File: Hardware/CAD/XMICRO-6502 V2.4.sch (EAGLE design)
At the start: 80 parts, among them Q1 2N4403, U1 74138, U10 7474, U11 74273, U12 74244, U13 74244, U14 74244, U15 74245, U16 74574, U17 7400, U18 7408, U19 7404, U2 74138, U20 W65C02S, U21 74244, U22 74138, U23 74148, U24 74244, U25 74244, U26 74273, U27 7432, U28 7432, U29 74257, U3 7400, U30 7474, U31 74LS14N, U4 7404, U5 74257, U6 74688, U7 74688, U8 74244, U9 7474, Y1 4MHz

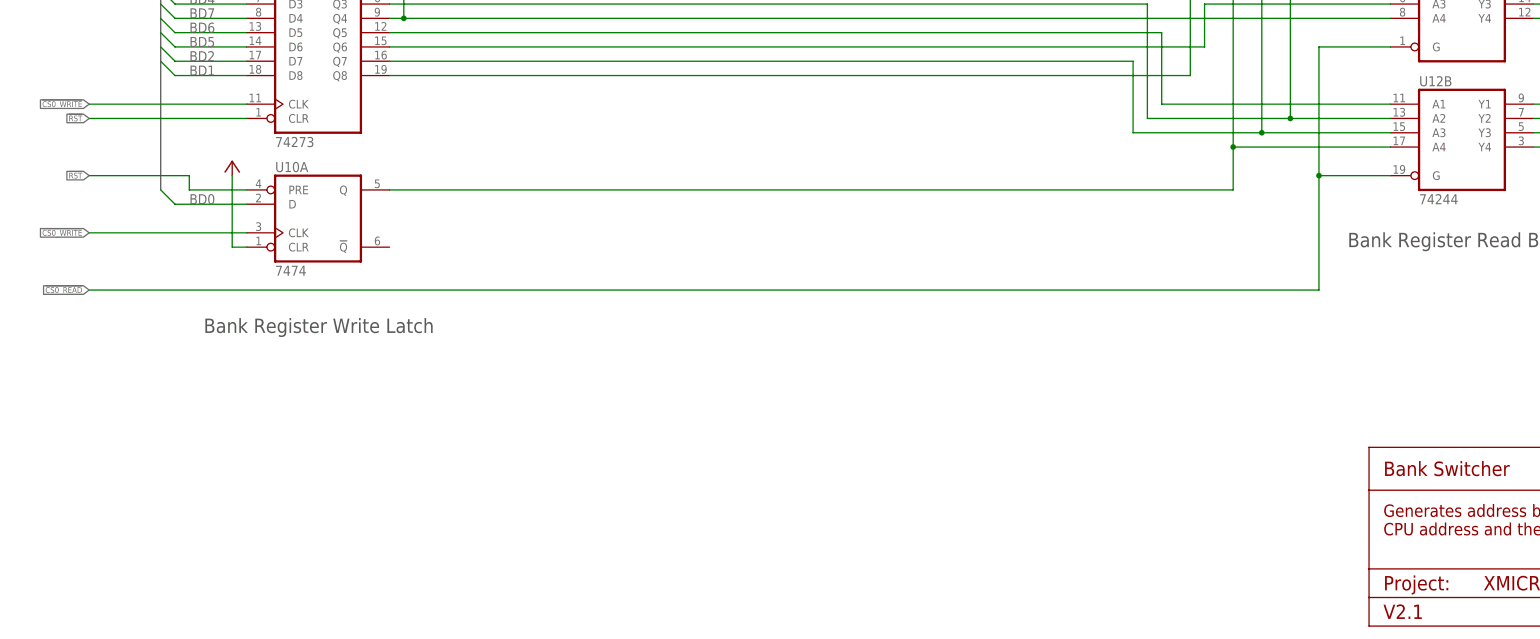
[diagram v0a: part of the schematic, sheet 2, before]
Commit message: Updated to V2.4 - made it necessary to manually clear DMA interrupts
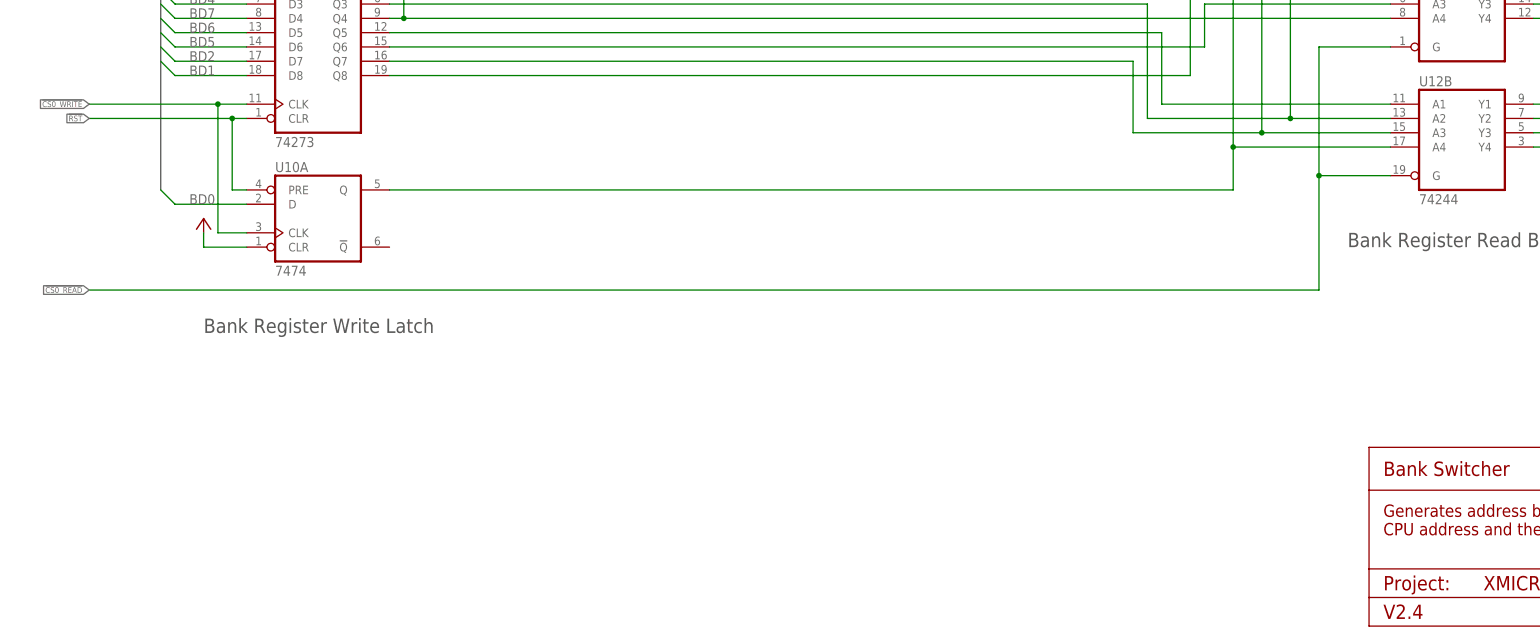
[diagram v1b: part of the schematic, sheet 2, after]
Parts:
- Y1: value 4MHz -> 12MHz
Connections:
- net !CS1_READ: now also U18B.I0
- net !IVP: no longer U18B.I0
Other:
- note added: "Interrupt is triggered upon !BUSACK!. Interrupt is cleared on reset or $X01 read (Interrupt Mask Register)"
- note added: "V2.4"
- note removed: "Interrupt is triggered upon !BUSACK!. Interrupt is cleared on reset or on the interrupt vector pull."
- note removed: "V2.1"
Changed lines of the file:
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@@
 <part name="GND12" library="supply1" deviceset="GND" device=""/>
 <part name="U17" library="74xx-us" deviceset="74*00" device="N" technology="LS" value="7400"/>
-<part name="Y1" library="Custom" deviceset="OSC-OE" device="" value="4MHz"/>
+<part name="Y1" library="Custom" deviceset="OSC-OE" device="" value="12MHz"/>
 <part name="P+1" library="supply1" deviceset="VCC" device=""/>
 <part name="GND14" library="supply1" deviceset="GND" device=""/>
@@
 <text x="306.07" y="10.16" size="2.54" layer="94" font="vector">Project:</text>
 <text x="306.07" y="30.48" size="2.54" layer="94" font="vector">CPU</text>
-<text x="306.07" y="5.08" size="2.54" layer="94" font="vector">V2.1</text>
+<text x="306.07" y="5.08" size="2.54" layer="94" font="vector">V2.4</text>
 <text x="379.73" y="10.16" size="2.54" layer="94" font="vector">Chris Weir</text>
 <text x="379.73" y="5.08" size="2.54" layer="94" font="vector">Sheet:</text>
@@
 <wire x1="402.59" y1="8.89" x2="377.19" y2="8.89" width="0" layer="94"/>
 <text x="306.07" y="10.16" size="2.54" layer="94" font="vector">Project:</text>
-<text x="306.07" y="5.08" size="2.54" layer="94" font="vector">V2.1</text>
+<text x="306.07" y="5.08" size="2.54" layer="94" font="vector">V2.4</text>
 <text x="379.73" y="10.16" size="2.54" layer="94" font="vector">Chris Weir</text>
 <text x="379.73" y="5.08" size="2.54" layer="94" font="vector">Sheet:</text>
@@
 <instance part="GND16" gate="1" x="236.22" y="167.64" smashed="yes"/>
 <instance part="U10" gate="A" x="116.84" y="76.2"/>
-<instance part="P+5" gate="VCC" x="101.6" y="86.36" smashed="yes"/>
+<instance part="P+5" gate="VCC" x="96.52" y="76.2" smashed="yes"/>
 <instance part="P+17" gate="VCC" x="101.6" y="124.46" smashed="yes"/>
 </instances>
@@
 <pinref part="U10" gate="A" pin="CLR"/>
 <pinref part="P+5" gate="VCC" pin="VCC"/>
-<wire x1="104.14" y1="71.12" x2="101.6" y2="71.12" width="0.1524" layer="91"/>
-<wire x1="101.6" y1="71.12" x2="101.6" y2="83.82" width="0.1524" layer="91"/>
+<wire x1="104.14" y1="71.12" x2="96.52" y2="71.12" width="0.1524" layer="91"/>
+<wire x1="96.52" y1="71.12" x2="96.52" y2="73.66" width="0.1524" layer="91"/>
 </segment>
 <segment>
@@
 <net name="!RST" class="0">
 <segment>
-<wire x1="104.14" y1="93.98" x2="76.2" y2="93.98" width="0.1524" layer="91"/>
+<wire x1="104.14" y1="93.98" x2="101.6" y2="93.98" width="0.1524" layer="91"/>
 <label x="76.2" y="93.98" size="1.016" layer="95" rot="R180" xref="yes"/>
 <pinref part="U11" gate="A" pin="CLR"/>
-<wire x1="104.14" y1="81.28" x2="93.98" y2="81.28" width="0.1524" layer="91"/>
-<wire x1="93.98" y1="81.28" x2="93.98" y2="83.82" width="0.1524" layer="91"/>
-<wire x1="93.98" y1="83.82" x2="76.2" y2="83.82" width="0.1524" layer="91"/>
-<label x="76.2" y="83.82" size="1.016" layer="95" rot="R180" xref="yes"/>
+<wire x1="101.6" y1="93.98" x2="76.2" y2="93.98" width="0.1524" layer="91"/>
+<wire x1="104.14" y1="81.28" x2="101.6" y2="81.28" width="0.1524" layer="91"/>
 <pinref part="U10" gate="A" pin="PRE"/>
+<wire x1="101.6" y1="81.28" x2="101.6" y2="93.98" width="0.1524" layer="91"/>
+<junction x="101.6" y="93.98"/>
 </segment>
 </net>
@@
 <segment>
 <pinref part="U11" gate="A" pin="CLK"/>
-<wire x1="76.2" y1="96.52" x2="104.14" y2="96.52" width="0.1524" layer="91"/>
+<wire x1="76.2" y1="96.52" x2="99.06" y2="96.52" width="0.1524" layer="91"/>
 <label x="76.2" y="96.52" size="1.016" layer="95" rot="R180" xref="yes"/>
-<wire x1="76.2" y1="73.66" x2="104.14" y2="73.66" width="0.1524" layer="91"/>
-<label x="76.2" y="73.66" size="1.016" layer="95" rot="R180" xref="yes"/>
+<wire x1="99.06" y1="96.52" x2="104.14" y2="96.52" width="0.1524" layer="91"/>
 <pinref part="U10" gate="A" pin="CLK"/>
+<wire x1="99.06" y1="73.66" x2="104.14" y2="73.66" width="0.1524" layer="91"/>
+<wire x1="99.06" y1="73.66" x2="99.06" y2="96.52" width="0.1524" layer="91"/>
+<junction x="99.06" y="96.52"/>
 </segment>
 </net>
@@
 <wire x1="402.59" y1="8.89" x2="377.19" y2="8.89" width="0" layer="94"/>
 <text x="306.07" y="10.16" size="2.54" layer="94" font="vector">Project:</text>
-<text x="306.07" y="5.08" size="2.54" layer="94" font="vector">V2.1</text>
+<text x="306.07" y="5.08" size="2.54" layer="94" font="vector">V2.4</text>
 <text x="379.73" y="10.16" size="2.54" layer="94" font="vector">Chris Weir</text>
 <text x="379.73" y="5.08" size="2.54" layer="94" font="vector">Sheet:</text>
@@
 <pinref part="U22" gate="A" pin="Y6"/>
 <wire x1="294.64" y1="104.14" x2="302.26" y2="104.14" width="0.1524" layer="91"/>
-<wire x1="302.26" y1="104.14" x2="312.42" y2="104.14" width="0.1524" layer="91"/>
-<junction x="302.26" y="104.14"/>
-<label x="320.04" y="104.14" size="1.016" layer="95" rot="R180" xref="yes"/>
 </segment>
 </net>
@@
 <description>DMA System</description>
 <plain>
-<text x="78.74" y="91.44" size="1.4224" layer="97" rot="MR180">Interrupt is triggered upon !BUSACK!.
-Interrupt is cleared on reset or on the interrupt vector pull.</text>
+<text x="76.2" y="93.98" size="1.4224" layer="97" rot="MR180">Interrupt is triggered upon !BUSACK!.
+Interrupt is cleared on reset or $X01 read (Interrupt Mask Register)</text>
 <frame x1="0" y1="0" x2="266.7" y2="203.2" columns="6" rows="5" layer="94"/>
 <text x="166.37" y="30.48" size="2.54" layer="94" font="vector">DMA System</text>
@@
 bus when safe, then acknowledges the request.
 An interrupt is triggered for each request.</text>
-<text x="78.74" y="96.52" size="2.54" layer="97" rot="MR180">DMA Interrupt</text>
+<text x="76.2" y="99.06" size="2.54" layer="97" rot="MR180">DMA Interrupt</text>
 <wire x1="163.83" y1="35.56" x2="262.89" y2="35.56" width="0" layer="94"/>
 <wire x1="262.89" y1="35.56" x2="262.89" y2="27.94" width="0" layer="94"/>
@@
 <wire x1="262.89" y1="8.89" x2="237.49" y2="8.89" width="0" layer="94"/>
 <text x="166.37" y="10.16" size="2.54" layer="94" font="vector">Project:</text>
-<text x="166.37" y="5.08" size="2.54" layer="94" font="vector">V2.1</text>
+<text x="166.37" y="5.08" size="2.54" layer="94" font="vector">V2.4</text>
 <text x="240.03" y="10.16" size="2.54" layer="94" font="vector">Chris Weir</text>
 <text x="240.03" y="5.08" size="2.54" layer="94" font="vector">Sheet:</text>
@@
 <text x="184.15" y="10.16" size="2.54" layer="94" font="vector">&gt;DRAWING_NAME</text>
 <text x="234.95" y="5.08" size="2.54" layer="94" font="vector" rot="MR0">&gt;LAST_DATE_TIME</text>
-<wire x1="76.2" y1="99.06" x2="76.2" y2="60.96" width="0.1524" layer="97" style="shortdash"/>
-<wire x1="76.2" y1="60.96" x2="187.96" y2="60.96" width="0.1524" layer="97" style="shortdash"/>
-<wire x1="187.96" y1="60.96" x2="187.96" y2="99.06" width="0.1524" layer="97" style="shortdash"/>
-<wire x1="187.96" y1="99.06" x2="76.2" y2="99.06" width="0.1524" layer="97" style="shortdash"/>
+<wire x1="73.66" y1="101.6" x2="73.66" y2="60.96" width="0.1524" layer="97" style="shortdash"/>
+<wire x1="73.66" y1="60.96" x2="187.96" y2="60.96" width="0.1524" layer="97" style="shortdash"/>
+<wire x1="187.96" y1="60.96" x2="187.96" y2="101.6" width="0.1524" layer="97" style="shortdash"/>
+<wire x1="187.96" y1="101.6" x2="73.66" y2="101.6" width="0.1524" layer="97" style="shortdash"/>
 </plain>
 <instances>
 <instance part="U10" gate="B" x="147.32" y="76.2"/>
 <instance part="U18" gate="B" x="109.22" y="71.12"/>
-<instance part="P+11" gate="VCC" x="132.08" y="86.36" smashed="yes" rot="MR0">
-<attribute name="VALUE" x="129.54" y="87.63" size="1.778" layer="96"/>
-</instance>
+<instance part="P+11" gate="VCC" x="132.08" y="86.36" smashed="yes" rot="MR0"/>
 <instance part="U9" gate="A" x="134.62" y="142.24"/>
-<instance part="P+16" gate="VCC" x="119.38" y="152.4" smashed="yes" rot="MR0">
-<attribute name="VALUE" x="116.84" y="153.67" size="1.778" layer="96"/>
-</instance>
+<instance part="P+16" gate="VCC" x="119.38" y="152.4" smashed="yes" rot="MR0"/>
 <instance part="U4" gate="E" x="66.04" y="149.86"/>
 <instance part="U18" gate="A" x="93.98" y="144.78"/>
 <instance part="U9" gate="B" x="193.04" y="142.24"/>
-<instance part="GND7" gate="1" x="177.8" y="132.08" rot="MR0"/>
+<instance part="GND7" gate="1" x="177.8" y="132.08" smashed="yes" rot="MR0"/>
 <instance part="U4" gate="F" x="66.04" y="129.54"/>
 <instance part="U4" gate="B" x="88.9" y="129.54"/>
@@
 </segment>
 </net>
-<net name="!IVP" class="0">
-<segment>
-<pinref part="U18" gate="B" pin="I0"/>
-<wire x1="96.52" y1="73.66" x2="88.9" y2="73.66" width="0.1524" layer="91"/>
-<label x="88.9" y="73.66" size="1.016" layer="95" rot="R180" xref="yes"/>
-</segment>
-</net>
 <net name="N$16" class="0">
 <segment>
@@
 </segment>
 </net>
+<net name="!CS1_READ" class="0">
+<segment>
+<pinref part="U18" gate="B" pin="I0"/>
+<wire x1="96.52" y1="73.66" x2="88.9" y2="73.66" width="0.1524" layer="91"/>
+<label x="88.9" y="73.66" size="1.016" layer="95" rot="R180" xref="yes"/>
+</segment>
+</net>
 </nets>
 </sheet>
@@
 <wire x1="262.89" y1="8.89" x2="237.49" y2="8.89" width="0" layer="94"/>
 <text x="166.37" y="10.16" size="2.54" layer="94" font="vector">Project:</text>
-<text x="166.37" y="5.08" size="2.54" layer="94" font="vector">V2.1</text>
+<text x="166.37" y="5.08" size="2.54" layer="94" font="vector">V2.4</text>
 <text x="240.03" y="10.16" size="2.54" layer="94" font="vector">Chris Weir</text>
 <text x="240.03" y="5.08" size="2.54" layer="94" font="vector">Sheet:</text>
@@
 <wire x1="262.89" y1="8.89" x2="237.49" y2="8.89" width="0" layer="94"/>
 <text x="166.37" y="10.16" size="2.54" layer="94" font="vector">Project:</text>
-<text x="166.37" y="5.08" size="2.54" layer="94" font="vector">V2.1</text>
+<text x="166.37" y="5.08" size="2.54" layer="94" font="vector">V2.4</text>
 <text x="240.03" y="10.16" size="2.54" layer="94" font="vector">Chris Weir</text>
 <text x="240.03" y="5.08" size="2.54" layer="94" font="vector">Sheet:</text>
